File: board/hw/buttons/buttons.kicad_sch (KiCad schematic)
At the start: 11 parts

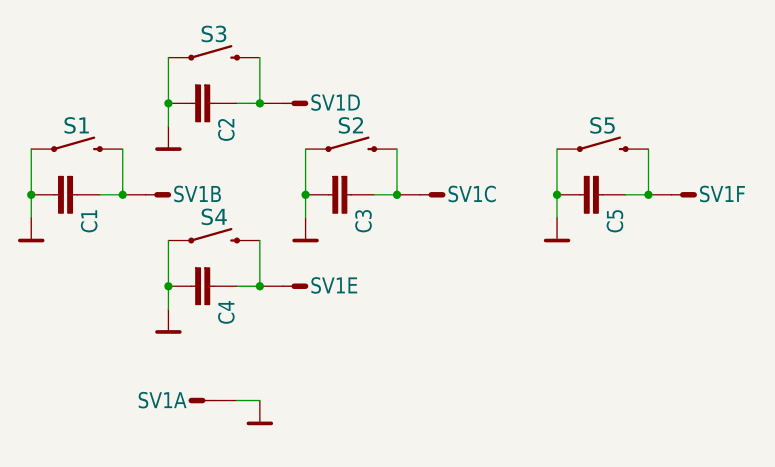
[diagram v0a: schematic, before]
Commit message: buttons board converted to newr KiCad
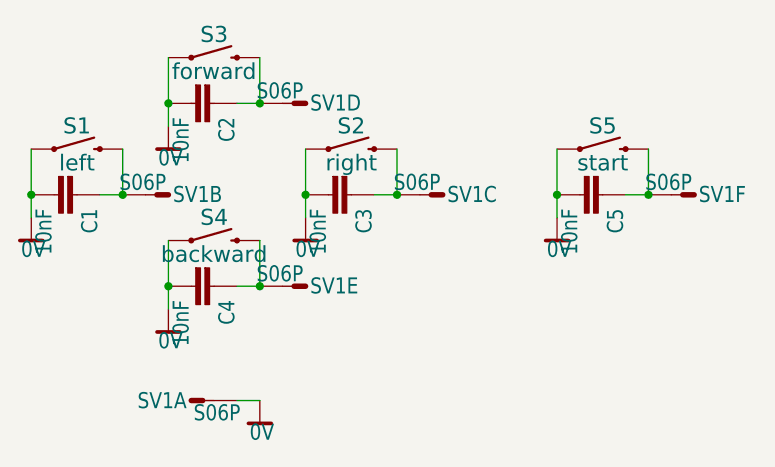
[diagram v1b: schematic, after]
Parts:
- C1, C2, C3, C4, C5: value (none) -> 10nF; footprint (none) -> buttons:C0805K
- S1: value (none) -> left; footprint (none) -> buttons:TACTILE_SWITCH_SMD_12MM
- S2: value (none) -> right; footprint (none) -> buttons:TACTILE_SWITCH_SMD_12MM
- S3: value (none) -> forward; footprint (none) -> buttons:TACTILE_SWITCH_SMD_12MM
- S4: value (none) -> backward; footprint (none) -> buttons:TACTILE_SWITCH_SMD_12MM
- S5: value (none) -> start; footprint (none) -> buttons:TACTILE_SWITCH_SMD_12MM
- SV1: value (none) -> S06P; footprint (none) -> buttons:S06P
